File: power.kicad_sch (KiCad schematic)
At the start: 0 parts

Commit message: edit README.md
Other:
- company: (none) -> NOIRLab
- title: (none) -> 4 channel ADC Module
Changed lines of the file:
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@@
 	(generator_version "9.0")
 	(paper "A4")
+	(title_block
+		(title "4 channel ADC Module")
+		(date "2025-04-18")
+		(rev "0.1")
+		(company "NOIRLab")
+		(comment 1 "Design: Braulio Cancino Vera - braulio.cancino@noirlab.edu")
+	)
 	(sheet
 		(at 140.97 33.02)

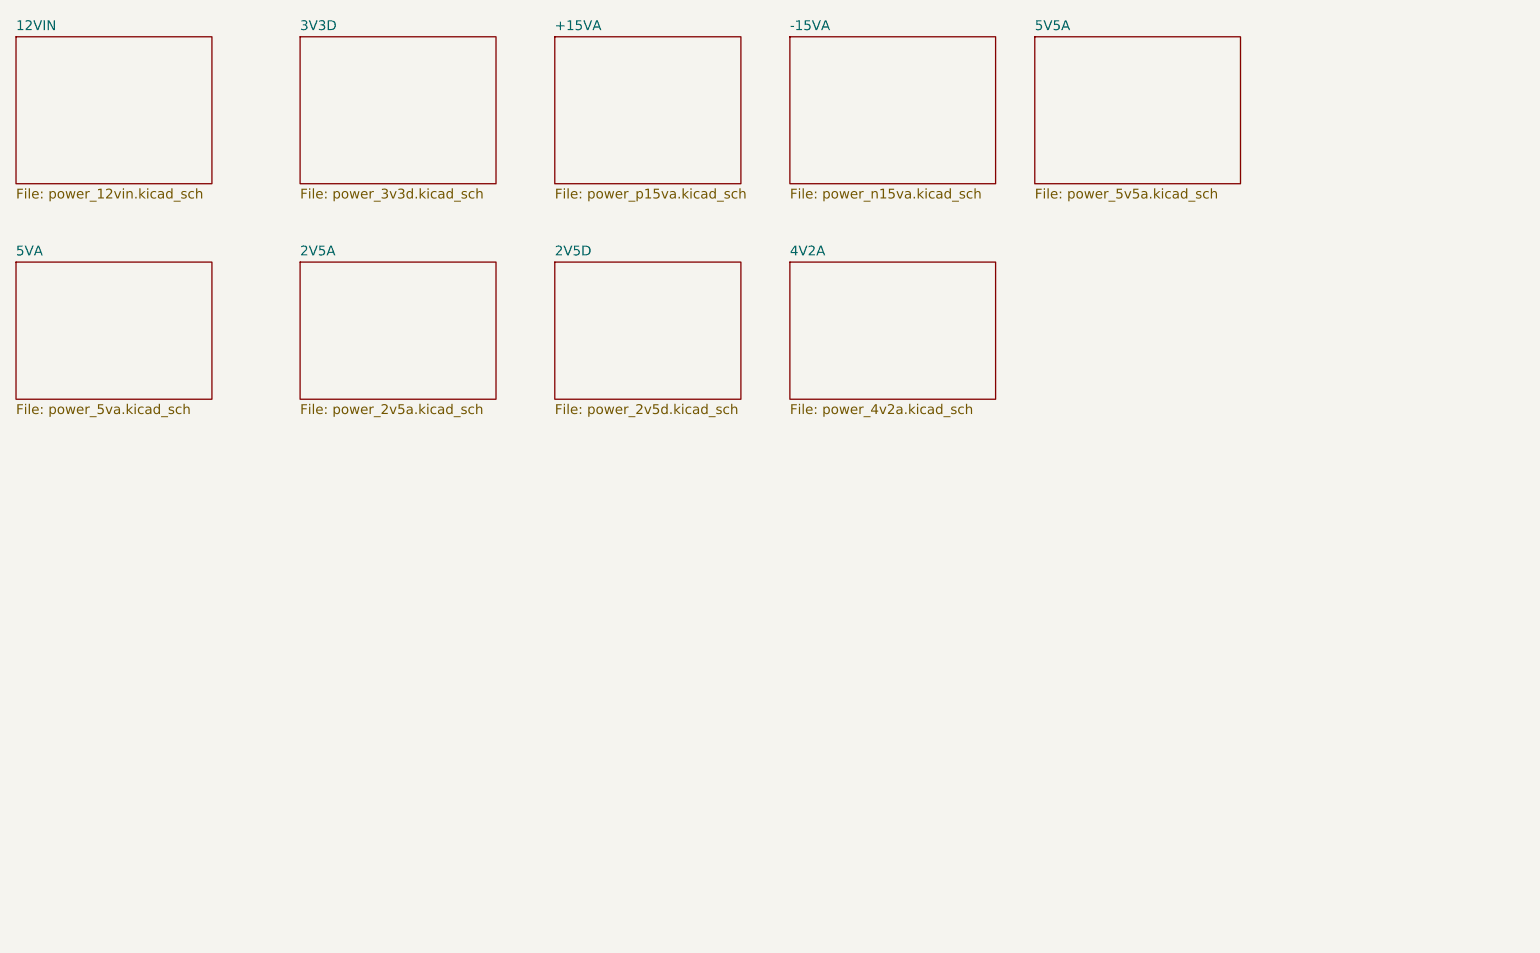
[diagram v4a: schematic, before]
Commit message: Split DC DC schematic and improve layout
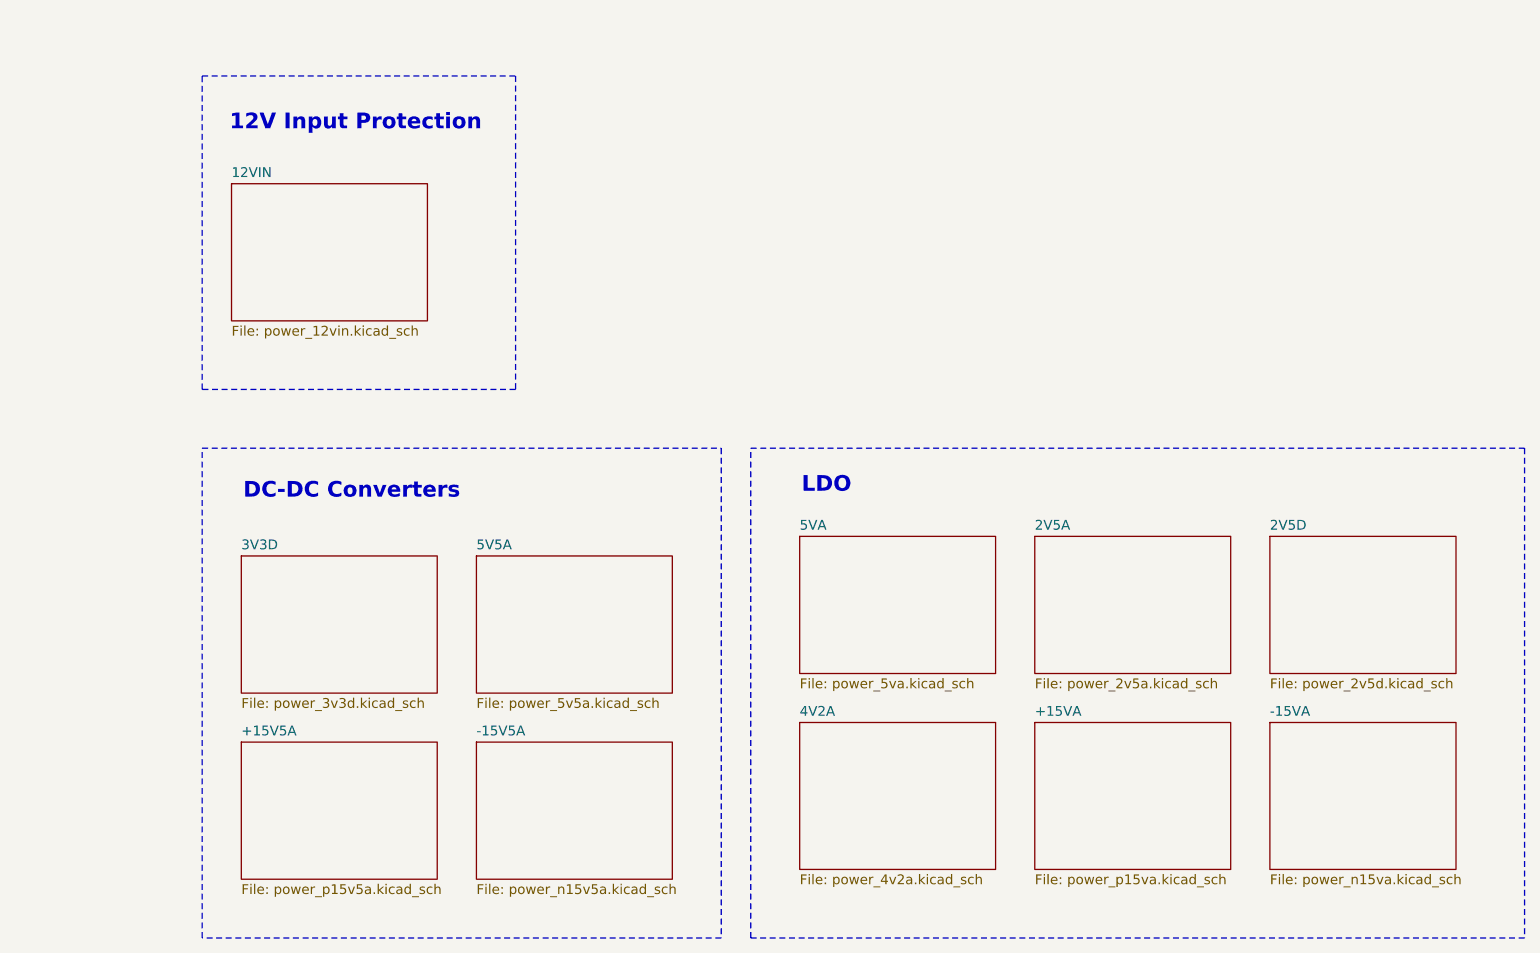
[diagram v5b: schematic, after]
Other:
- added sheet +15V5A (power_p15v5a.kicad_sch)
- added sheet -15V5A (power_n15v5a.kicad_sch)
- note added: "12V Input Protection"
- note added: "DC-DC Converters"
- note added: "LDO"
